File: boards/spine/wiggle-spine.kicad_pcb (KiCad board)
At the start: 2 copper layers, 177 parts, among them CON1 5-24V 5A, CON2 5-24V 16A, CON3 PLR135, CON4 PLT133, CON5 USB-B, CON6 XLR-3 Female, CON7 USB-A, Q1 IRFML8244, Q2 IRFML8244, Q3 IRFML8244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

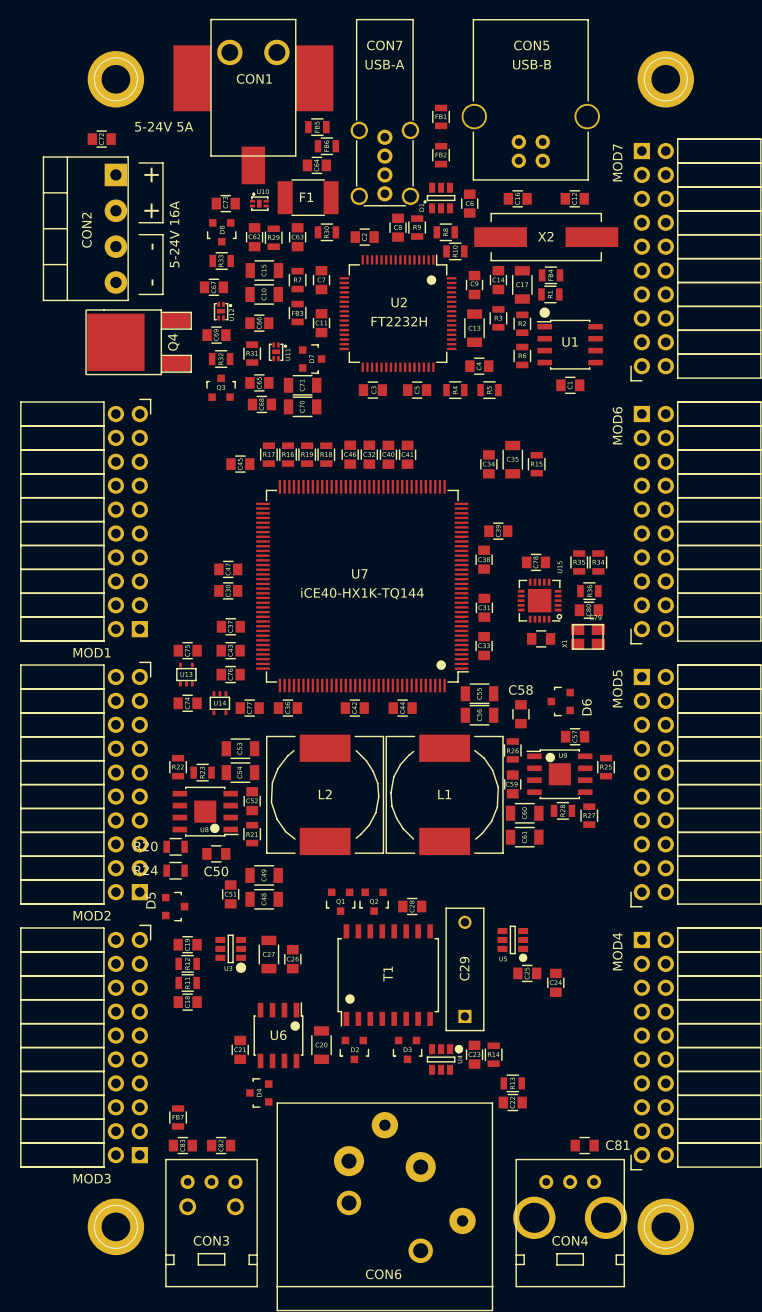
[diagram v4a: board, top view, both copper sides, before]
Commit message: Adjust holes, pmod spacing, rounded corners
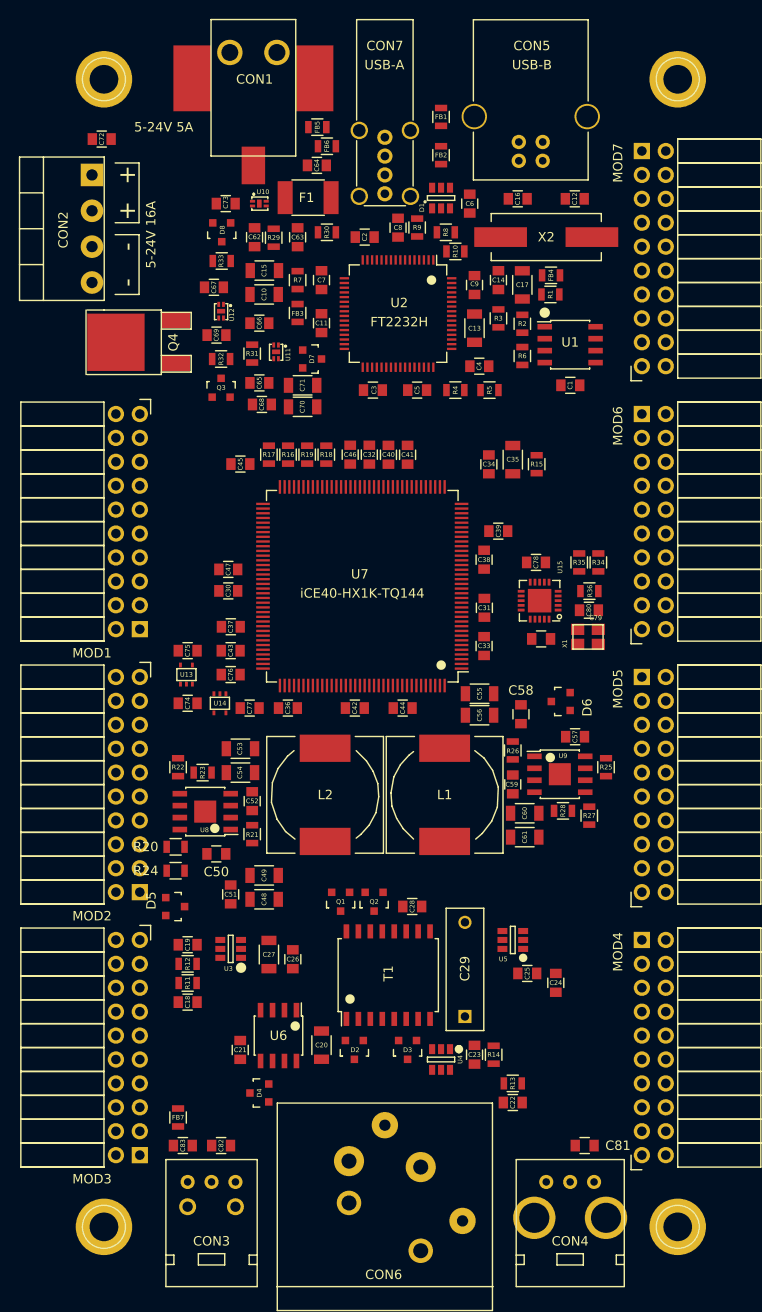
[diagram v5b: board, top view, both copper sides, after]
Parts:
- moved CON2 2.54 mm to (64.7, 85.1)
- moved REF** 1.27 mm to (73.7, 196.8)
- moved REF** 1.27 mm to (134.6, 196.8)
- moved REF** 1.27 mm to (134.6, 74.9)
- moved REF** 1.27 mm to (73.7, 74.9)
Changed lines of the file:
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@@
     (links 605)
     (no_connects 605)
-    (area 22.184999 -6.920001 142.915001 243.280001)
+    (area 64.094999 59.38 165.785715 206.715)
     (thickness 1.6)
-    (drawings 7)
+    (drawings 11)
     (tracks 0)
     (zones 0)
@@
   )
   (module Connect:1pin (layer F.Cu)
-    (at 74.93 196.85)
+    (at 73.66 196.85)
     (descr "module 1 pin (ou trou mecanique de percage)")
     (tags DEV)
@@
   )
   (module Connect:1pin (layer F.Cu)
-    (at 133.35 196.85)
+    (at 134.62 196.85)
     (descr "module 1 pin (ou trou mecanique de percage)")
     (tags DEV)
@@
   )
   (module Connect:1pin (layer F.Cu)
-    (at 133.35 74.93)
+    (at 134.62 74.93)
     (descr "module 1 pin (ou trou mecanique de percage)")
     (tags DEV)
@@
   )
   (module Connect:1pin (layer F.Cu)
-    (at 74.93 74.93)
+    (at 73.66 74.93)
     (descr "module 1 pin (ou trou mecanique de percage)")
     (tags DEV)
@@
   )
   (module Terminal_Blocks:TerminalBlock_Pheonix_PT-3.5mm_4pol (layer F.Cu)
-    (at 67.23 85.09 270)
+    (at 64.69 85.09 270)
     (descr "4-way 3.5mm pitch terminal block, Phoenix PT series")
     (fp_text reference CON2 (at 5.842 -4.652 270) (layer F.SilkS)
@@
     )
   )
+  (gr_arc (start 134.62 193.04) (end 143.51 193.04) (angle 90) (layer F.Fab) (width 0.2))
+  (gr_arc (start 73.66 193.04) (end 73.66 201.93) (angle 90) (layer F.Fab) (width 0.2))
+  (gr_arc (start 73.66 78.74) (end 64.77 78.74) (angle 90) (layer F.Fab) (width 0.2))
+  (gr_arc (start 134.62 78.74) (end 134.62 69.85) (angle 90) (layer F.Fab) (width 0.2))
   (dimension 27.94 (width 0.3) (layer F.SilkS)
     (gr_text "1.1000 in" (at 160.1 96.52 270) (layer F.SilkS)
@@
       (effects (font (size 1.5 1.5) (thickness 0.3)))
     )
-    (feature1 (pts (xy 138.43 201.93) (xy 153.83 201.93)))
-    (feature2 (pts (xy 138.43 69.85) (xy 153.83 69.85)))
+    (feature1 (pts (xy 134.62 201.93) (xy 153.83 201.93)))
+    (feature2 (pts (xy 134.62 69.85) (xy 153.83 69.85)))
     (crossbar (pts (xy 151.13 69.85) (xy 151.13 201.93)))
     (arrow1a (pts (xy 151.13 201.93) (xy 150.543579 200.803496)))
@@
     (arrow2b (pts (xy 151.13 69.85) (xy 151.716421 70.976504)))
   )
-  (dimension 68.58 (width 0.3) (layer F.SilkS)
-    (gr_text "2.7000 in" (at 104.14 60.88) (layer F.SilkS)
+  (dimension 78.74 (width 0.3) (layer F.SilkS)
+    (gr_text "3.1000 in" (at 104.14 59.931436) (layer F.SilkS)
       (effects (font (size 1.5 1.5) (thickness 0.3)))
     )
-    (feature1 (pts (xy 138.43 69.85) (xy 138.43 59.53)))
-    (feature2 (pts (xy 69.85 69.85) (xy 69.85 59.53)))
-    (crossbar (pts (xy 69.85 62.23) (xy 138.43 62.23)))
-    (arrow1a (pts (xy 138.43 62.23) (xy 137.303496 62.816421)))
-    (arrow1b (pts (xy 138.43 62.23) (xy 137.303496 61.643579)))
-    (arrow2a (pts (xy 69.85 62.23) (xy 70.976504 62.816421)))
-    (arrow2b (pts (xy 69.85 62.23) (xy 70.976504 61.643579)))
-  )
-  (gr_line (start 69.85 69.85) (end 69.85 201.93) (layer F.Fab) (width 0.2))
-  (gr_line (start 138.43 69.85) (end 69.85 69.85) (layer F.Fab) (width 0.2))
-  (gr_line (start 138.43 201.93) (end 138.43 69.85) (layer F.Fab) (width 0.2))
-  (gr_line (start 69.85 201.93) (end 138.43 201.93) (layer F.Fab) (width 0.2))
+    (feature1 (pts (xy 143.51 77.47) (xy 143.51 58.581436)))
+    (feature2 (pts (xy 64.77 77.47) (xy 64.77 58.581436)))
+    (crossbar (pts (xy 64.77 61.281436) (xy 143.51 61.281436)))
+    (arrow1a (pts (xy 143.51 61.281436) (xy 142.383496 61.867857)))
+    (arrow1b (pts (xy 143.51 61.281436) (xy 142.383496 60.695015)))
+    (arrow2a (pts (xy 64.77 61.281436) (xy 65.896504 61.867857)))
+    (arrow2b (pts (xy 64.77 61.281436) (xy 65.896504 60.695015)))
+  )
+  (gr_line (start 64.77 78.74) (end 64.77 193.04) (layer F.Fab) (width 0.2))
+  (gr_line (start 134.62 69.85) (end 73.66 69.85) (layer F.Fab) (width 0.2))
+  (gr_line (start 143.51 193.04) (end 143.51 78.74) (layer F.Fab) (width 0.2))
+  (gr_line (start 73.66 201.93) (end 134.62 201.93) (layer F.Fab) (width 0.2))
 )

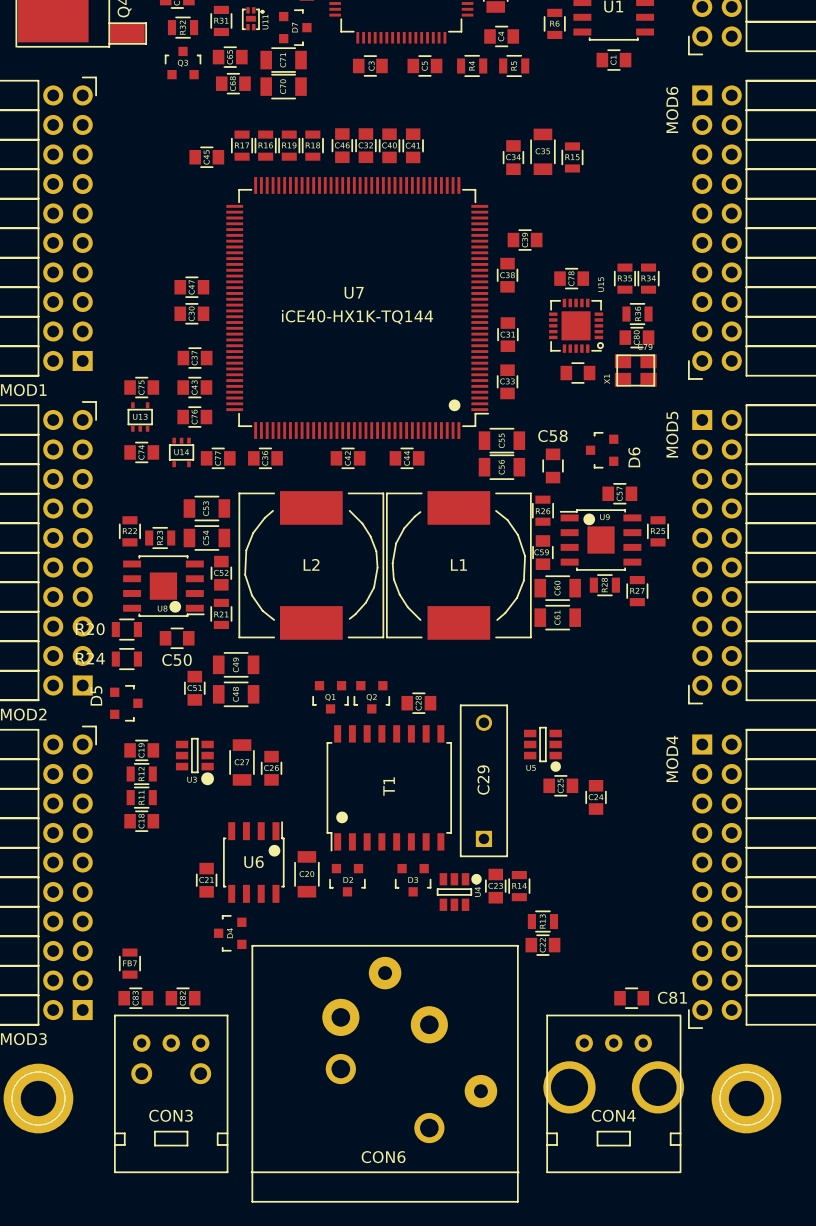
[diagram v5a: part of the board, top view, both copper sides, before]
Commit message: Save room for a Wiggleport logo
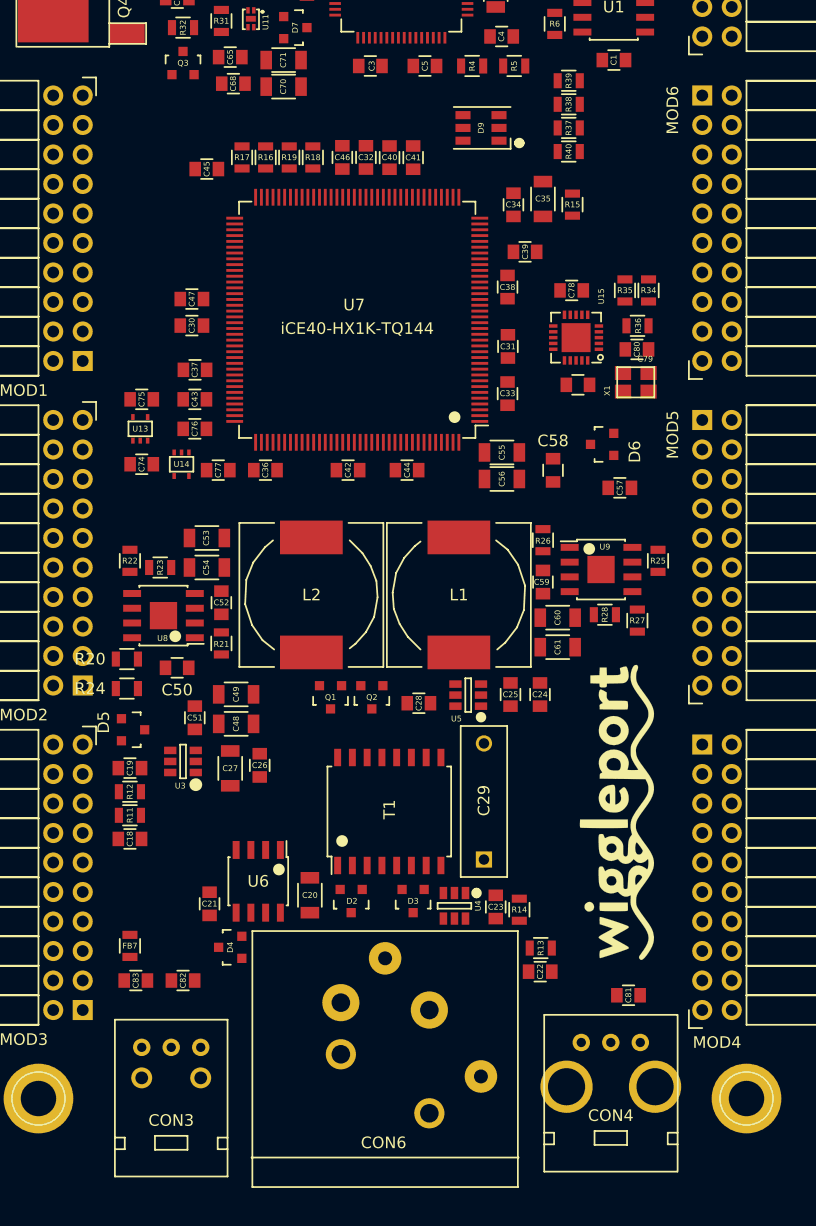
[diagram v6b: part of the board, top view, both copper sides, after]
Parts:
- added D9: LED_BGR, LEDs:LED_RGB_PLLC-6, F.Cu at (111.8, 113.3)
- added G***: LOGO, Wiggleport:wiggleport-wordmark, F.Cu at (77.2, 218.4)
- added G***: LOGO, Wiggleport:wiggleport-wordmark, F.Cu at (71.1, 218.9)
- added G***: LOGO, Wiggleport:wiggleport-wordmark, F.Cu at (123.4, 172.2)
- added R37: 750, Resistors_SMD:R_0805, F.Cu at (119.3, 113.3)
- added R38: 750, Resistors_SMD:R_0805, F.Cu at (119.3, 111.3)
- added R39: 240, Resistors_SMD:R_0805, F.Cu at (119.3, 109.2)
- added R40: 10k, Resistors_SMD:R_0805, F.Cu at (119.3, 115.3)
- moved C24 10.1 mm to (116.8, 162.1)
- moved C25 8.97 mm to (114.3, 162.1), turned to 270 degrees
- moved U5 7.71 mm to (110.7, 162.1)
- moved R15 4.06 mm to (119.6, 119.9)
- moved C34 4.06 mm to (114.6, 119.9)
- moved C35 4.06 mm to (117.1, 119.4)
- moved C48 2.54 mm to (90.7, 164.6)
- moved C51 2.54 mm to (87.1, 164.1)
- moved C60 2.54 mm to (118.4, 155.4)
- moved R21 2.54 mm to (89.4, 157.7)
- moved R22 2.54 mm to (81.5, 150.6)
- moved R24 2.54 mm to (81.3, 161.6)
- moved R25 2.54 mm to (127.0, 150.6)
- moved U8 2.54 mm to (84.4, 155.3)
- moved C49 2.54 mm to (90.7, 162.1)
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
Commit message: Nudge
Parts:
- moved G*** 1.14 mm to (122.9, 173.2)
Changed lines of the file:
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@@
 (kicad_pcb (version 4) (host pcbnew 4.0.0-rc2-1-stable)
   (general
-    (links 0)
+    (links 613)
     (no_connects 613)
-    (area 0 0 0 0)
+    (area 64.094999 58.431436 165.785715 220.3648)
     (thickness 1.6)
     (drawings 11)
@@
     (descr "Through hole socket strip")
     (tags "socket strip")
-    (fp_text reference MOD1 (at 25.4 5.08 540) (layer F.SilkS)
+    (fp_text reference MOD1 (at 0.254 -2.286 270) (layer F.SilkS)
       (effects (font (size 1 1) (thickness 0.15)))
     )
@@
   )
   (module Wiggleport:wiggleport-wordmark (layer F.Cu)
-    (at 123.444 172.212 90)
+    (at 122.936 173.228 90)
     (fp_text reference G*** (at 0 0 90) (layer F.SilkS) hide
       (effects (font (thickness 0.3)))
